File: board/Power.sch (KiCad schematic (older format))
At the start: 115 parts, among them CON1 BARREL_JACK, CON2 BARREL_JACK, P1 CONN_2, U12 TPS51200, U4 GBU15005-G, U5 7805, U6 TPS54560, U7 TPS53319, U8 TPS54625, U9 TPS54625

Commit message: Issue #1481 - DOC
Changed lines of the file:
@@
 LIBS:contrib
 LIBS:valves
+LIBS:hdmi2usb
 LIBS:HDMI2USB-cache
+LIBS:Atlys-VHDCI-cache
 EELAYER 27 0
 EELAYER END
 $Descr A3 16535 11693
 encoding utf-8
-Sheet 4 11
+Sheet 4 12
 Title "HDMI2USB"
-Date "14 jan 2015"
+Date "18 feb 2015"
 Rev "Rev2"
 Comp ""
@@
 $EndComp
 $Comp
-L GND #PWR15
+L GND #PWR08
 U 1 1 52DD9648
 P 11300 7700
-F 0 "#PWR15" H 11300 7700 30  0001 C CNN
+F 0 "#PWR08" H 11300 7700 30  0001 C CNN
 F 1 "GND" H 11300 7630 30  0001 C CNN
 F 2 "" H 11300 7700 60  0000 C CNN
@@
 $EndComp
 $Comp
-L GND #PWR19
+L GND #PWR09
 U 1 1 52DD9786
 P 12800 5350
-F 0 "#PWR19" H 12800 5350 30  0001 C CNN
+F 0 "#PWR09" H 12800 5350 30  0001 C CNN
 F 1 "GND" H 12800 5280 30  0001 C CNN
 F 2 "" H 12800 5350 60  0000 C CNN
@@
 $EndComp
 $Comp
-L GND #PWR18
+L GND #PWR010
 U 1 1 52DD9A04
 P 11500 1100
-F 0 "#PWR18" H 11500 1100 30  0001 C CNN
+F 0 "#PWR010" H 11500 1100 30  0001 C CNN
 F 1 "GND" H 11500 1030 30  0001 C CNN
 F 2 "" H 11500 1100 60  0000 C CNN
@@
 $EndComp
 $Comp
-L GND #PWR10
+L GND #PWR011
 U 1 1 52DD9A0A
 P 9400 2950
-F 0 "#PWR10" H 9400 2950 30  0001 C CNN
+F 0 "#PWR011" H 9400 2950 30  0001 C CNN
 F 1 "GND" H 9400 2880 30  0001 C CNN
 F 2 "" H 9400 2950 60  0000 C CNN
@@
 $EndComp
 $Comp
-L GND #PWR8
+L GND #PWR012
 U 1 1 52E1FEA6
 P 4000 1950
-F 0 "#PWR8" H 4000 1950 30  0001 C CNN
+F 0 "#PWR012" H 4000 1950 30  0001 C CNN
 F 1 "GND" H 4000 1880 30  0001 C CNN
 F 2 "" H 4000 1950 60  0000 C CNN
@@
 $EndComp
 $Comp
-L GND #PWR14
+L GND #PWR013
 U 1 1 52E4CA76
 P 10900 8600
-F 0 "#PWR14" H 10900 8600 30  0001 C CNN
+F 0 "#PWR013" H 10900 8600 30  0001 C CNN
 F 1 "GND" H 10900 8530 30  0001 C CNN
 F 2 "" H 10900 8600 60  0000 C CNN
@@
 $EndComp
 $Comp
-L GND #PWR11
+L GND #PWR014
 U 1 1 52E4CA88
 P 10450 9800
-F 0 "#PWR11" H 10450 9800 30  0001 C CNN
+F 0 "#PWR014" H 10450 9800 30  0001 C CNN
 F 1 "GND" H 10450 9730 30  0001 C CNN
 F 2 "" H 10450 9800 60  0000 C CNN
@@
 $EndComp
 $Comp
-L GND #PWR23
+L GND #PWR015
 U 1 1 52E4CAA0
 P 13800 9800
-F 0 "#PWR23" H 13800 9800 30  0001 C CNN
+F 0 "#PWR015" H 13800 9800 30  0001 C CNN
 F 1 "GND" H 13800 9730 30  0001 C CNN
 F 2 "" H 13800 9800 60  0000 C CNN
@@
 $EndComp
 $Comp
-L GND #PWR22
+L GND #PWR016
 U 1 1 52E4CAAC
 P 13200 9300
-F 0 "#PWR22" H 13200 9300 30  0001 C CNN
+F 0 "#PWR016" H 13200 9300 30  0001 C CNN
 F 1 "GND" H 13200 9230 30  0001 C CNN
 F 2 "" H 13200 9300 60  0000 C CNN
@@
 $EndComp
 $Comp
-L GND #PWR16
+L GND #PWR017
 U 1 1 52E4CAB8
 P 11350 9950
-F 0 "#PWR16" H 11350 9950 30  0001 C CNN
+F 0 "#PWR017" H 11350 9950 30  0001 C CNN
 F 1 "GND" H 11350 9880 30  0001 C CNN
 F 2 "" H 11350 9950 60  0000 C CNN
@@
 VCC3V3
 $Comp
-L GND #PWR20
+L GND #PWR018
 U 1 1 52E4CABF
 P 12800 9700
-F 0 "#PWR20" H 12800 9700 30  0001 C CNN
+F 0 "#PWR018" H 12800 9700 30  0001 C CNN
 F 1 "GND" H 12800 9630 30  0001 C CNN
 F 2 "" H 12800 9700 60  0000 C CNN
@@
 $EndComp
 $Comp
-L GND #PWR21
+L GND #PWR019
 U 1 1 52E4CACB
 P 13100 9950
-F 0 "#PWR21" H 13100 9950 30  0001 C CNN
+F 0 "#PWR019" H 13100 9950 30  0001 C CNN
 F 1 "GND" H 13100 9880 30  0001 C CNN
 F 2 "" H 13100 9950 60  0000 C CNN
@@
 $EndComp
 $Comp
-L GND #PWR12
+L GND #PWR020
 U 1 1 52F26CB0
 P 10650 3700
-F 0 "#PWR12" H 10650 3700 30  0001 C CNN
+F 0 "#PWR020" H 10650 3700 30  0001 C CNN
 F 1 "GND" H 10650 3630 30  0001 C CNN
 F 2 "" H 10650 3700 60  0000 C CNN
@@
 $EndComp
 $Comp
-L GND #PWR13
+L GND #PWR021
 U 1 1 52F2BB58
 P 10900 6200
-F 0 "#PWR13" H 10900 6200 30  0001 C CNN
+F 0 "#PWR021" H 10900 6200 30  0001 C CNN
 F 1 "GND" H 10900 6130 30  0001 C CNN
 F 2 "" H 10900 6200 60  0000 C CNN
@@
 $EndComp
 $Comp
-L GND #PWR17
+L GND #PWR022
 U 1 1 52F2C00C
 P 11450 6150
-F 0 "#PWR17" H 11450 6150 30  0001 C CNN
+F 0 "#PWR022" H 11450 6150 30  0001 C CNN
 F 1 "GND" H 11450 6080 30  0001 C CNN
 F 2 "" H 11450 6150 60  0000 C CNN
@@
 Connection ~ 13350 2900
 Wire Wire Line
-	13650 1750 14400 1750
+	13650 1750 14950 1750
 Connection ~ 13650 1750
 Wire Wire Line
@@
 Wire Wire Line
 	12550 6250 14850 6250
-Wire Wire Line
-	14400 1750 14950 1750
 Connection ~ 14200 1750
 Connection ~ 3900 1450
@@
 Connection ~ 7400 1800
 $Comp
-L GND #PWR9
+L GND #PWR023
 U 1 1 533EEA66
 P 7400 2850
-F 0 "#PWR9" H 7400 2850 30  0001 C CNN
+F 0 "#PWR023" H 7400 2850 30  0001 C CNN
 F 1 "GND" H 7400 2780 30  0001 C CNN
 F 2 "" H 7400 2850 60  0000 C CNN
@@
 Text Label 14750 3900 2    59   ~ 0
 VCC1V5
-Connection ~ 4250 8450
-Connection ~ 3850 8900
-Wire Wire Line
-	4250 8900 4250 8850
-Connection ~ 3250 8900
-Wire Wire Line
-	3850 8900 3850 8850
-Connection ~ 3850 8450
-Wire Wire Line
-	3650 8450 4350 8450
-Connection ~ 2750 8900
-Connection ~ 2750 8450
-Wire Wire Line
-	2750 8500 2750 8450
-Wire Wire Line
-	2450 8450 2450 8500
-Wire Wire Line
-	2850 8450 2450 8450
+Text Notes 1050 7700 0    79   ~ 16
+VCC5V0
+Wire Notes Line
+	900  7750 6750 7750
+Wire Notes Line
+	6750 7750 6750 9650
+Wire Notes Line
+	6750 9650 900  9650
+Wire Notes Line
+	900  9650 900  7750
+Text GLabel 4350 8450 2    60   Output ~ 0
+VCC5V0
+$Comp
+L 7805 U5
+U 1 1 5499621B
+P 3250 8500
+F 0 "U5" H 3400 8304 60  0000 C CNN
+F 1 "7805" H 3250 8700 60  0000 C CNN
+F 2 "~" H 3250 8500 60  0000 C CNN
+F 3 "~" H 3250 8500 60  0000 C CNN
+	1    3250 8500
+	1    0    0    -1
+$EndComp
+Text Label 3150 8900 2    39   ~ 0
+GND
+Wire Wire Line
+	3250 8900 3250 8750
+Wire Wire Line
+	2450 8900 4250 8900
+$Comp
+L C C47
+U 1 1 54996452
+P 2750 8700
+F 0 "C47" H 2800 8800 50  0000 L CNN
+F 1 "4.7uF" H 2750 8600 50  0000 L CNN
+F 2 "" H 2750 8700 60  0000 C CNN
+F 3 "" H 2750 8700 60  0000 C CNN
+	1    2750 8700
+	-1   0    0    1
+$EndComp
+$Comp
+L C C49
+U 1 1 54996464
+P 3850 8650
+F 0 "C49" H 3900 8750 50  0000 L CNN
+F 1 "47uF" H 3850 8550 50  0000 L CNN
+F 2 "" H 3850 8650 60  0000 C CNN
+F 3 "" H 3850 8650 60  0000 C CNN
+	1    3850 8650
+	-1   0    0    1
+$EndComp
+$Comp
+L C C50
+U 1 1 5499646A
+P 4250 8650
+F 0 "C50" H 4300 8750 50  0000 L CNN
+F 1 "47uF" H 4250 8550 50  0000 L CNN
+F 2 "" H 4250 8650 60  0000 C CNN
+F 3 "" H 4250 8650 60  0000 C CNN
+	1    4250 8650
+	-1   0    0    1
+$EndComp
 $Comp
 L C C46
@@
 	-1   0    0    1
 $EndComp
-$Comp
-L C C50
-U 1 1 5499646A
-P 4250 8650
-F 0 "C50" H 4300 8750 50  0000 L CNN
-F 1 "47uF" H 4250 8550 50  0000 L CNN
-F 2 "" H 4250 8650 60  0000 C CNN
-F 3 "" H 4250 8650 60  0000 C CNN
-	1    4250 8650
-	-1   0    0    1
-$EndComp
-$Comp
-L C C49
-U 1 1 54996464
-P 3850 8650
-F 0 "C49" H 3900 8750 50  0000 L CNN
-F 1 "47uF" H 3850 8550 50  0000 L CNN
-F 2 "" H 3850 8650 60  0000 C CNN
-F 3 "" H 3850 8650 60  0000 C CNN
-	1    3850 8650
-	-1   0    0    1
-$EndComp
-$Comp
-L C C47
-U 1 1 54996452
-P 2750 8700
-F 0 "C47" H 2800 8800 50  0000 L CNN
-F 1 "4.7uF" H 2750 8600 50  0000 L CNN
-F 2 "" H 2750 8700 60  0000 C CNN
-F 3 "" H 2750 8700 60  0000 C CNN
-	1    2750 8700
-	-1   0    0    1
-$EndComp
-Wire Wire Line
-	2450 8900 4250 8900
-Wire Wire Line
-	3250 8900 3250 8750
-Text Label 3150 8900 2    39   ~ 0
-GND
-$Comp
-L 7805 U5
-U 1 1 5499621B
-P 3250 8500
-F 0 "U5" H 3400 8304 60  0000 C CNN
-F 1 "7805" H 3250 8700 60  0000 C CNN
-F 2 "~" H 3250 8500 60  0000 C CNN
-F 3 "~" H 3250 8500 60  0000 C CNN
-	1    3250 8500
-	1    0    0    -1
-$EndComp
-Text GLabel 4350 8450 2    60   Output ~ 0
-VCC5V0
-Wire Notes Line
-	900  9650 900  7750
-Wire Notes Line
-	6750 9650 900  9650
-Wire Notes Line
-	6750 7750 6750 9650
-Wire Notes Line
-	900  7750 6750 7750
-Text Notes 1050 7700 0    79   ~ 16
-VCC5V0
+Wire Wire Line
+	2850 8450 2450 8450
+Wire Wire Line
+	2450 8450 2450 8500
+Wire Wire Line
+	2750 8500 2750 8450
+Connection ~ 2750 8450
+Connection ~ 2750 8900
+Wire Wire Line
+	3650 8450 4350 8450
+Connection ~ 3850 8450
+Wire Wire Line
+	3850 8900 3850 8850
+Connection ~ 3250 8900
+Wire Wire Line
+	4250 8900 4250 8850
+Connection ~ 3850 8900
+Connection ~ 4250 8450
 $EndSCHEMATC

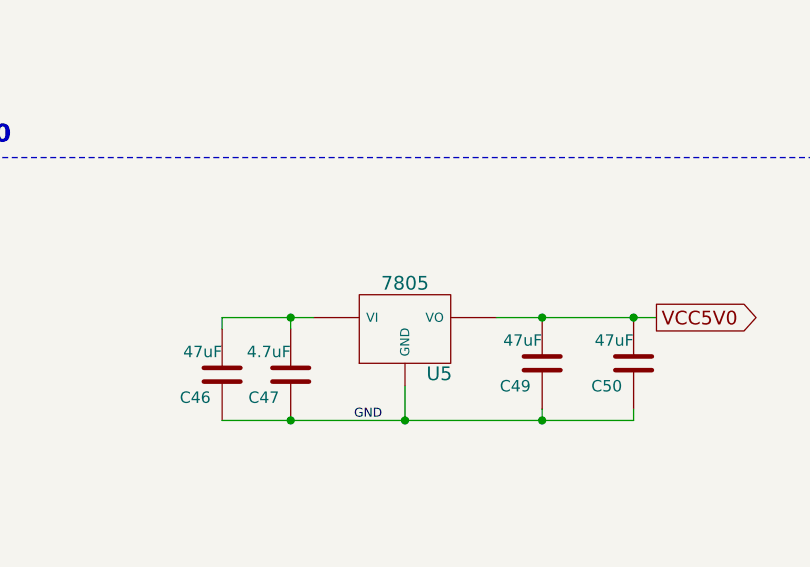
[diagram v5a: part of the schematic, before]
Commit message: Issue #1412 - Placement on 6-3-15
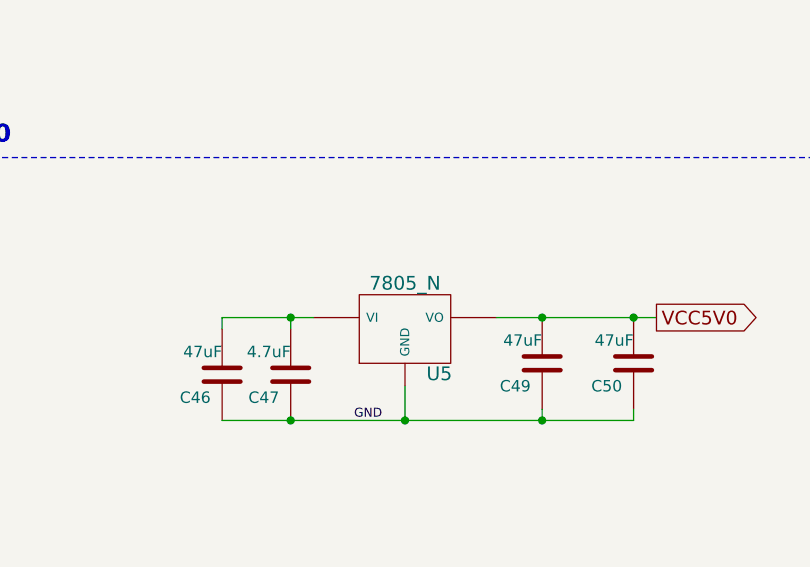
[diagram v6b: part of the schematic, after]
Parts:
- removed U5: 7805, ~, symbol 7805
- added U5: 7805_N, ~, symbol 7805_N
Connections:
- net GND: now also U5.2 (GND)
- net VCC5V0: now also U5.3 (VO)
- net at C46.2, C47.2: now also U5.1 (VI)
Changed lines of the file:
@@
 Sheet 3 12
 Title "HDMI2USB"
-Date "2 mar 2015"
+Date "5 mar 2015"
 Rev "Rev2"
 Comp ""
@@
 Text GLabel 4350 8450 2    60   Output ~ 0
 VCC5V0
-$Comp
-L 7805 U5
-U 1 1 5499621B
-P 3250 8500
-F 0 "U5" H 3400 8304 60  0000 C CNN
-F 1 "7805" H 3250 8700 60  0000 C CNN
-F 2 "~" H 3250 8500 60  0000 C CNN
-F 3 "~" H 3250 8500 60  0000 C CNN
-	1    3250 8500
-	1    0    0    -1
-$EndComp
 Text Label 3150 8900 2    39   ~ 0
 GND
@@
 Connection ~ 3850 8900
 Connection ~ 4250 8450
+$Comp
+L 7805_N U5
+U 1 1 54F86042
+P 3250 8500
+F 0 "U5" H 3400 8304 60  0000 C CNN
+F 1 "7805_N" H 3250 8700 60  0000 C CNN
+F 2 "~" H 3250 8500 60  0000 C CNN
+F 3 "~" H 3250 8500 60  0000 C CNN
+	1    3250 8500
+	1    0    0    -1
+$EndComp
 $EndSCHEMATC
